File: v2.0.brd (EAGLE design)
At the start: 245 x 105 mm, 283 parts, among them J1 DC-044-A, J10 16p-2.54, J11 16p-2.54, J2 MICROSD-9P, J3 2p-2.54, J4 2p-2.54, J5 16p-2.54, J6 16p-2.54, J7 16p-2.54, J8 2p-2.54, J9 16p-2.54, Q1 32.768khZ@6Pf, Q2 SSM3J328R,LF, Q3 BSS138W-7-F, Q4 BSS138W-7-F, Q5 SSM3J328R,LF, Q6 BSS138W-7-F, Q7 BSS138W-7-F, Q8 CJ2305, SW1 MK-12C02 G1.5, SW3 MK-12C02 G1.5, SW4 MK-12C02 G1.5, SW5 TS-1101F, U1 MCP23017-E/SO, U10 74HCT139D, U11 BZX84C30, U12 SP483ECN-L, U13 FT232RL-SSOP28, U14 FT232RL-SSOP28, U15 FT232RL-SSOP28, U2 MCP79412-I/SN, U3 LOPY, U4 MAX213IDBR, U5 FT232RL-SSOP28, U6 FT232RL-SSOP28, U8 BR24G32-3, Y2 12MHZ

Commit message: Start of mods for V2
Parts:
- removed SW5: TS-1101F, Seeed-Switch-2016:SW2-5.0-6.0X3.0X4.3MM
- added SW2: MK-12C02 G1.5, Seeed-Switch:SW7-SMD-L6.7X2.7X3.2MM
- F1: device Seeed-OPL-2017-01-Fuse-Akita:TH_5MM_14MM -> imported-parts:TH_5MM_14MM
- moved J4 3.81 mm to (-15.0, 24.1)
- turned Q2 to 90 degrees
- flipped U$7 to the top
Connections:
- net +5V: now also Q2.2; no longer Q2.3
- net 5V_USB_HUB_FERRITE: now also SW2.A; no longer SW5.2
- net FTDI_HUB_LEDS: now also SW2.COM; no longer SW5.1
- net GND: now also SW2.SS1, SW2.SS2, SW2.SS3, SW2.SS4
- net N$122: now also Q2.3; no longer Q2.2
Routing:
- net GPIO4: track 81.2 -> 88.1 mm
- net LOPY_MISO: track 111.7 -> 115.5 mm
- net LOPY_3V3: track 228.5 -> 232.3 mm
- net N$123: track 11.4 -> 14.9 mm
- net N$122: track 5.47 -> 7.27 mm
- net PI_5V: track 491.2 -> 489.9 mm
- net 5V_USB_HUB_FERRITE: track 206.1 -> 204.9 mm
- net +3V3: track 672.6 -> 671.5 mm, vias 26 -> 27
- net +5V: track 434.3 -> 433.4 mm
- net FTDI_HUB_LEDS: track 60.0 -> 60.5 mm
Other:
- board text added: "3V3 Smth"
- board text added: "Pi 3V3"
- board text added: "Pi 5V"
- board text added: "SPI0"
- board text added: "V2.0"
- board text removed: "SPI8"
- board text removed: "V1.0"

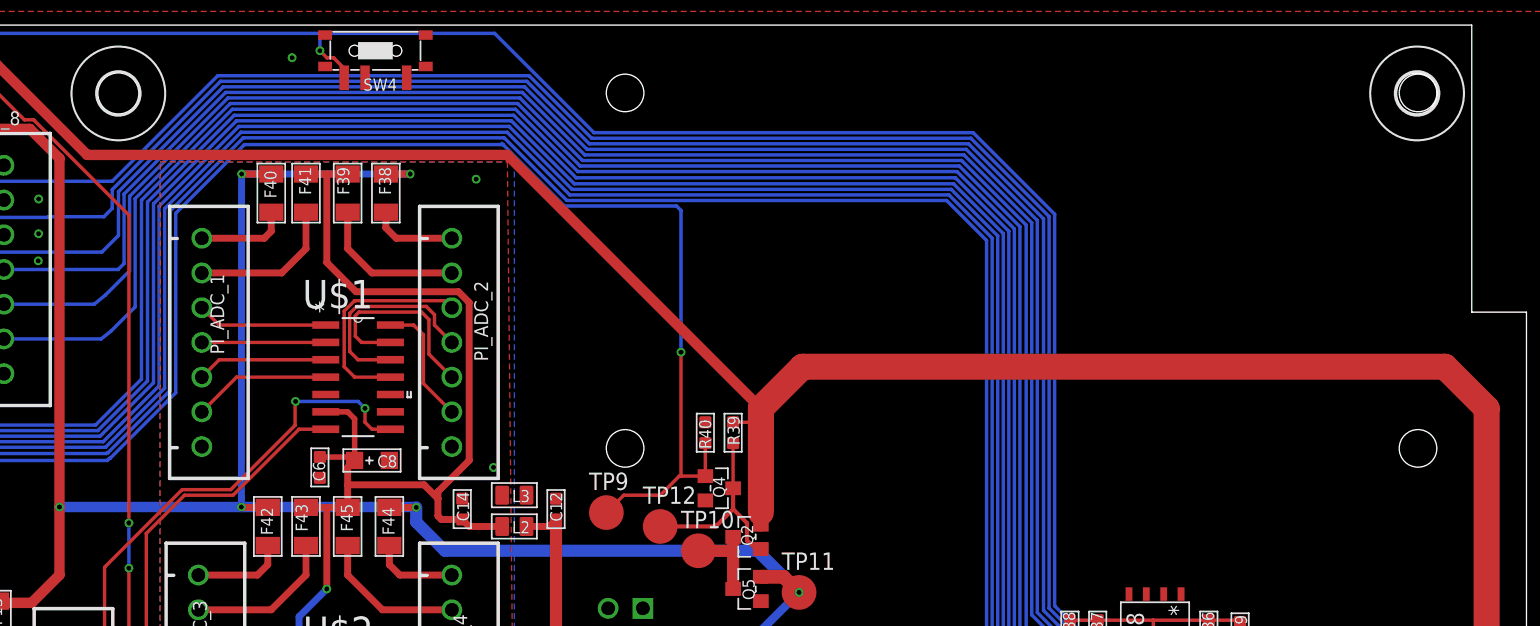
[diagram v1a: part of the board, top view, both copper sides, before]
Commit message: moved some test pads around
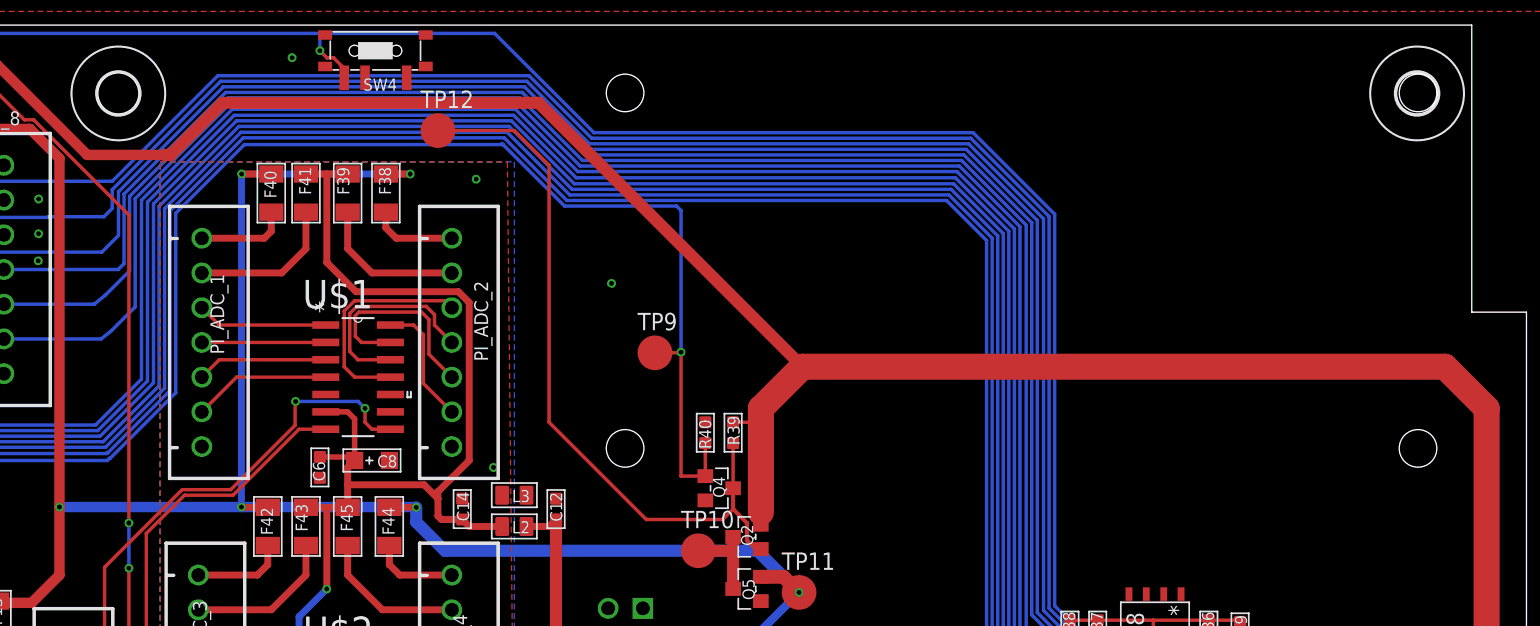
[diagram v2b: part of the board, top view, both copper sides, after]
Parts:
- moved TP12 33.2 mm to (103.4, 97.3)
- moved TP9 12.2 mm to (119.3, 81.0)
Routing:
- net N$123: track 14.9 -> 53.5 mm
- net +5V: track 433.4 -> 438.3 mm
- net PI_PWR_CTRL: track 266.4 -> 261.8 mm
- net GND: vias 46 -> 47

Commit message: More work on fixing bugs
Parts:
- added Q10, Q9: S8550, Seeed-Transistor:SOT-23
- added R26: 10K, Seeed-Resistor:R0603
- added R47: 47K, Seeed-Resistor:R0603
- moved Q8 0.51 mm to (-33.3, 32.5)
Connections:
- new net N$14: Q10.1, Q10.3, Q9.1, R26.2
- new net N$15: Q5.1, Q9.3, R47.2
- net GND: now also R26.1, R47.1; no longer Q5.1
- net LOPY_3V3: now also Q8.2; no longer Q8.3
- net LOPY_MISO: now also Q8.3; no longer Q8.2
- net N$122: now also Q10.2
- net PI_5V: now also Q9.2
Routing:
- net N$15: track 0.00 -> 8.99 mm
- net N$14: track 0.00 -> 7.88 mm
- net PI_5V: track 489.9 -> 496.5 mm, vias 6 -> 7
- net N$122: track 7.27 -> 10.3 mm
- net LOPY_3V3: track 232.3 -> 230.2 mm, vias 8 -> 9
- net LOPY_MISO: track 115.5 -> 116.9 mm

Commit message: fixed name of pycom pin 12 signal track
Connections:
- net GPIO16 renamed GPIO6

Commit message: More updates to fix issues and start of v2 BOM
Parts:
- F1: value 307010005_DIP_PPTC_4A_0310 -> (none); device imported-parts:TH_5MM_14MM -> imported-parts:2920
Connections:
- removed net LOPY_P23: J7.6, J9.6, U3.P$25
- new net LOPY_USD_SCLK: J2.5, U3.P$25
- net +24V: now also U$3.2; no longer U$3.1
- net +24V_UNREG_IN: now also F1.1; no longer F1.P$1
- net +5V: now also SW3.B
- net GND: now also U$3.1; no longer U$3.2
- net LOPY_3V3: no longer SW3.B
- net LOPY_3V3_FUSED: now also J7.6, J9.6; no longer J7.3, J9.3
- net LOPY_5V_FUSED: now also J7.3, J9.3
- net LOPY_CS1: now also J2.7; no longer LOPY_SPI.3
- net LOPY_CS2: now also LOPY_SPI.3; no longer J2.2
- net LOPY_MISO: no longer J2.7
- net LOPY_MOSI: no longer J2.3
- net LOPY_RXD1: now also J2.3
- net LOPY_SCL/CLK: no longer J2.5
- net N$68: now also F1.2; no longer F1.P$2
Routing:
- net +5V: track 438.3 -> 516.5 mm, vias 1 -> 2
- net LOPY_USD_SCLK: track 0.00 -> 46.4 mm, vias 0 -> 2
- net LOPY_RXD1: track 53.0 -> 98.2 mm, vias 0 -> 2
- net LOPY_CS2: track 19.5 -> 63.6 mm
- net LOPY_CS1: track 70.5 -> 33.6 mm, vias 0 -> 2
- net LOPY_SCL/CLK: track 97.5 -> 67.5 mm, vias 1 -> 0
- net LOPY_3V3: track 230.2 -> 200.8 mm, vias 9 -> 10
- net LOPY_MOSI: track 97.1 -> 70.9 mm, vias 1 -> 0
- net LOPY_MISO: track 116.9 -> 99.2 mm
- net LOPY_P23: track 13.7 -> 0.00 mm
- net LOPY_5V_FUSED: track 19.5 -> 24.6 mm
- net LOPY_3V3_FUSED: track 28.4 -> 33.0 mm
- net +24V: track 61.4 -> 63.9 mm
- net PI_PWR_CTRL: track 261.8 -> 264.0 mm, vias 4 -> 5
- net LED_GND: track 582.4 -> 584.4 mm
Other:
- outline, holes or cut-outs redrawn
- board text removed: "23"

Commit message: More updates, and verifing of current state of BOM
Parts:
- C31: device Seeed-Capacitor:C0805 -> Seeed-Capacitor:C0603
- C40, C44, C48: value 47uf -> 4.7uf; device Seeed-Capacitor-2016:AVX-A -> Seeed-Capacitor:AVX-A
- F1: value (none) -> 1A
- R2: value 10K 1/10W -> 10K
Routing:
- net GND: vias 47 -> 52
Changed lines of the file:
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@@
 <attribute name="VALUE" x="13.081" y="11.811" size="0.635" layer="27" ratio="10" rot="R90"/>
 </element>
-<element name="C31" library="Seeed-Capacitor" library_urn="urn:adsk.eagle:library:464" package="C0805" value="100nf" x="42.5072" y="2.282" smashed="yes" rot="R270">
-<attribute name="MPN" value="CC0805KRX7R9BB104" x="42.5072" y="2.282" size="1.778" layer="27" rot="R270" display="off"/>
+<element name="C31" library="Seeed-Capacitor" package="C0603" value="100nf" x="42.5072" y="2.282" smashed="yes" rot="R270">
+<attribute name="MPN" value="CC0603KRX7R9BB104" x="42.5072" y="2.282" size="1.778" layer="27" rot="R270" display="off"/>
 <attribute name="NAME" x="43.9042" y="2.663" size="0.889" layer="25" font="vector" ratio="11" rot="R180"/>
 <attribute name="VALUE" x="44.4122" y="4.441" size="0.635" layer="27" ratio="10" rot="R180"/>
@@
 <attribute name="VALUE" x="189.103" y="19.685" size="0.635" layer="27" ratio="10" rot="R180"/>
 </element>
-<element name="C40" library="Seeed-Capacitor-2016" package="AVX-A" value="47uf" x="10.922" y="18.796" smashed="yes" rot="R90">
-<attribute name="MPN" value="TAJA476*006#NJ" x="10.922" y="18.796" size="1.778" layer="27" rot="R90" display="off"/>
+<element name="C40" library="Seeed-Capacitor" package="AVX-A" value="4.7uf" x="10.922" y="18.796" smashed="yes" rot="R90">
+<attribute name="MPN" value="TAJA475*016#NJ" x="10.922" y="18.796" size="1.778" layer="27" rot="R90" display="off"/>
 <attribute name="NAME" x="9.906" y="17.653" size="0.889" layer="25" ratio="11" rot="R90"/>
-<attribute name="VALUE" x="13.081" y="16.891" size="0.635" layer="27" ratio="10" rot="R90"/>
+<attribute name="VALUE" value="4.7uf" x="13.081" y="16.891" size="0.635" layer="27" ratio="10" rot="R90"/>
 </element>
 <element name="C42" library="Seeed-Capacitor-2016" package="C0603" value="100nf" x="4.318" y="39.878" smashed="yes" rot="R270">
@@
 <attribute name="VALUE" x="0.3175" y="32.004" size="0.635" layer="27" ratio="10" rot="R90"/>
 </element>
-<element name="C44" library="Seeed-Capacitor-2016" package="AVX-A" value="47uf" x="4.318" y="37.846" smashed="yes">
-<attribute name="MPN" value="TAJA476*006#NJ" x="4.318" y="37.846" size="1.778" layer="27" display="off"/>
+<element name="C44" library="Seeed-Capacitor" package="AVX-A" value="4.7uf" x="4.318" y="37.846" smashed="yes">
+<attribute name="MPN" value="TAJA475*016#NJ" x="4.318" y="37.846" size="1.778" layer="27" display="off"/>
 <attribute name="NAME" x="6.985" y="37.338" size="0.889" layer="25" ratio="11"/>
-<attribute name="VALUE" x="2.413" y="35.687" size="0.635" layer="27" ratio="10"/>
+<attribute name="VALUE" value="4.7uf" x="2.413" y="35.687" size="0.635" layer="27" ratio="10"/>
 </element>
 <element name="C46" library="Seeed-Capacitor-2016" package="C0603" value="100nf" x="18.034" y="40.386" smashed="yes" rot="R270">
@@
 <attribute name="VALUE" x="10.668" y="31.9405" size="0.635" layer="27" ratio="10"/>
 </element>
-<element name="C48" library="Seeed-Capacitor-2016" package="AVX-A" value="47uf" x="18.034" y="38.354" smashed="yes">
-<attribute name="MPN" value="TAJA476*006#NJ" x="18.034" y="38.354" size="1.778" layer="27" display="off"/>
+<element name="C48" library="Seeed-Capacitor" package="AVX-A" value="4.7uf" x="18.034" y="38.354" smashed="yes">
+<attribute name="MPN" value="TAJA475*016#NJ" x="18.034" y="38.354" size="1.778" layer="27" display="off"/>
 <attribute name="NAME" x="13.335" y="37.846" size="0.889" layer="25" ratio="11"/>
-<attribute name="VALUE" x="16.129" y="36.195" size="0.635" layer="27" ratio="10"/>
+<attribute name="VALUE" value="4.7uf" x="16.129" y="36.195" size="0.635" layer="27" ratio="10"/>
 </element>
 <element name="C6" library="Seeed-Capacitor-2016" library_urn="urn:adsk.eagle:library:450" package="C0603" value="100nf" x="94.742" y="72.644" smashed="yes" rot="R180">
@@
 <attribute name="VALUE" x="88.5825" y="22.987" size="0.635" layer="27" ratio="10" rot="R270"/>
 </element>
-<element name="F1" library="imported-parts" package="2920" value="" x="182.626" y="35.306" rot="R270"/>
+<element name="F1" library="imported-parts" package="2920" value="1A" x="182.626" y="35.306" rot="R270"/>
 <element name="F2" library="Seeed-Fuse" library_urn="urn:adsk.eagle:library:469" package="F1206" value="SMD1206R500SF" x="-0.508" y="96.012" smashed="yes" rot="R270">
 <attribute name="MPN" value="SMD1206R500SF" x="-0.508" y="96.012" size="1.778" layer="27" rot="R270" display="off"/>
@@
 <attribute name="VALUE" x="123.025" y="59.009" size="0.635" layer="27" ratio="10" rot="R270"/>
 </element>
-<element name="R2" library="Seeed-Resistor" library_urn="urn:adsk.eagle:library:474" package="R0603" value="10K 1/10W" x="143.51" y="25.4" smashed="yes" rot="R180">
-<attribute name="MPN" value="RC0603JR-0710KL" x="143.51" y="25.4" size="1.778" layer="27" rot="R180" display="off"/>
+<element name="R2" library="Seeed-Resistor" package="R0603" value="10K" x="143.51" y="25.4" smashed="yes" rot="R180">
+<attribute name="MPN" value="RC0603FR-0710KL" x="143.51" y="25.4" size="1.778" layer="27" rot="R180" display="off"/>
 <attribute name="NAME" x="143.002" y="26.543" size="0.889" layer="25" ratio="11" rot="R270"/>
-<attribute name="VALUE" x="142.075" y="27.005" size="0.635" layer="27" ratio="10" rot="R270"/>
+<attribute name="VALUE" value="10K" x="142.075" y="27.005" size="0.635" layer="27" ratio="10" rot="R270"/>
 </element>
 <element name="R20" library="Seeed-Resistor" library_urn="urn:adsk.eagle:library:474" package="R0603" value="15K 1/10W" x="183.134" y="20.066" smashed="yes" rot="R90">
@@
 <contactref element="R26" pad="1"/>
 <contactref element="R47" pad="1"/>
+<via x="142.24" y="54.61" extent="1-16" drill="0.35"/>
+<via x="147.066" y="60.071" extent="1-16" drill="0.35"/>
+<via x="123.571" y="38.989" extent="1-16" drill="0.35"/>
+<via x="125.857" y="38.608" extent="1-16" drill="0.35"/>
+<via x="125.73" y="27.686" extent="1-16" drill="0.35"/>
 </signal>
 <signal name="+3V3">
@@
 <wire x1="21.082" y1="9.906" x2="20.574" y2="10.414" width="0.254" layer="1"/>
 <wire x1="23.114" y1="8.128" x2="21.844" y2="8.128" width="0.254" layer="1"/>
-<wire x1="41.6182" y1="2.282" x2="41.6182" y2="1.9942" width="0.254" layer="1"/>
+<wire x1="41.7452" y1="2.282" x2="41.6182" y2="1.9942" width="0.254" layer="1"/>
 <wire x1="41.6182" y1="1.9942" x2="40.386" y2="0.762" width="0.254" layer="1"/>
 <wire x1="22.4412" y1="19.427" x2="23.753" y2="19.427" width="0.254" layer="1"/>
@@
 <contactref element="SW2" pad="A"/>
 <wire x1="46.736" y1="3.756" x2="43.0922" y2="3.756" width="0.254" layer="1"/>
-<wire x1="43.0922" y1="3.756" x2="41.6182" y2="2.282" width="0.254" layer="1"/>
+<wire x1="43.0922" y1="3.756" x2="41.7452" y2="2.282" width="0.254" layer="1"/>
 </signal>
 <signal name="N$49">

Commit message: Lopy reset and bootloader now on port expander
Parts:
- added F56, F57: SMD1206R500SF, Seeed-Fuse:F1206
- moved R2 23.8 mm to (120.0, 21.5)
- moved J6 4.83 mm to (134.9, 5.59), turned to 270 degrees
- moved J5 3.17 mm to (134.9, 2.16), turned to 270 degrees
- moved R8 0.89 mm to (-31.8, 56.0)
- moved R41 0.25 mm to (-30.2, 48.8), turned to 0 degrees
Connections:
- removed net GPIO_3V3_FUSED: F62.2, J10.4, J10.5, J10.6, J11.4, J11.5, J11.6
- removed net GPIO_EXP_0: J5.1, J6.1, U1.21
- removed net GPIO_EXP_1: J5.2, J6.2, U1.22
- removed net GPIO_EXP_10: J5.11, J6.11, U1.3
- removed net GPIO_EXP_11: J5.12, J6.12, U1.4
- removed net GPIO_EXP_12: J5.13, J6.13, U1.5
- removed net GPIO_EXP_13: J5.14, J6.14, U1.6
- removed net GPIO_EXP_14: J5.15, J6.15, U1.7
- removed net GPIO_EXP_15: J5.16, J6.16, U1.8
- removed net GPIO_EXP_2: J5.3, J6.3, U1.23
- removed net GPIO_EXP_3: J5.4, J6.4, U1.24
- removed net GPIO_EXP_4: J5.5, J6.5, U1.25
- removed net GPIO_EXP_5: J5.6, J6.6, U1.26
- removed net GPIO_EXP_6: J5.7, J6.7, U1.27
- removed net GPIO_EXP_7: J5.8, J6.8, U1.28
- removed net GPIO_EXP_8: J5.9, J6.9, U1.1
- removed net GPIO_EXP_9: J5.10, J6.10, U1.2
- new net EXP_3V3: F56.1, J5.2, J6.2
- new net EXP_5V: F57.1, J5.1, J6.1
- new net GPA0: J5.3, J6.3, U1.21
- new net GPA1: J5.4, J6.4, U1.22
- new net GPA2: J5.5, J6.5, U1.23
- new net GPA3: J5.6, J6.6, U1.24
- new net GPA4: J5.7, J6.7, U1.25
- new net GPA5: J5.8, J6.8, U1.26
- new net GPA6: J5.9, J6.9, U1.27
- new net GPA7: J5.10, J6.10, U1.28
- new net GPB0: J5.11, J6.11, U1.1
- new net GPB1: J5.12, J6.12, U1.2
- new net GPB2: J5.13, J6.13, U1.3
- new net GPB3: J5.14, J6.14, U1.4
- new net GPB4: J5.15, J6.15, U1.5
- new net GPIO26: J10.14, J11.14, PCB1.P$37
- new net N$16: R41.1, U1.6
- new net N$18: R17.1, U1.7
- new net N$19: F62.2, J10.3, J10.4, J11.3, J11.4
- net +3V3: now also F56.2
- net GND: now also J5.16, J6.16; no longer J10.14, J11.14
- net GPIO5: now also J10.5, J11.5; no longer R41.2
- net GPIO6: now also J10.6, J11.6; no longer R17.2
- net GPIO_5V_FUSED: no longer J10.3, J11.3
- net LOPY_RST_EN: now also U1.8; no longer PCB1.P$37
- net P12_SIG: now also R17.2; no longer R17.1
- net P2_SIG: now also R41.2; no longer R41.1
- net PI_5V: now also F57.2
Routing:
- net N$18: track 0.00 -> 403.7 mm, vias 0 -> 2
- net N$16: track 0.00 -> 378.5 mm, vias 0 -> 2
- net GPIO6: track 305.5 -> 47.7 mm
- net GPIO5: track 266.9 -> 46.4 mm
- net LOPY_RST_EN: track 267.8 -> 367.8 mm, vias 3 -> 4
- net GPIO_EXP_8: track 51.6 -> 0.00 mm
- net GPIO_EXP_9: track 48.8 -> 0.00 mm
- net GPB4: track 0.00 -> 48.3 mm
- net GPIO_EXP_10: track 45.5 -> 0.00 mm
- net GPB3: track 0.00 -> 43.6 mm
- net GPIO_EXP_11: track 41.8 -> 0.00 mm
- net PI_5V: track 496.5 -> 536.8 mm, vias 7 -> 9
- net GPIO_EXP_0: track 40.1 -> 0.00 mm
- net GPIO_EXP_12: track 39.0 -> 0.00 mm
- net GPIO26: track 0.00 -> 39.0 mm
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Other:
- board text added: "26"
- board text added: "GPA0"
- board text added: "GPA1"
- board text added: "GPA2"
- board text added: "GPA3"
- board text added: "GPA4"
- board text added: "GPA5"
- board text added: "GPA6"
- board text added: "GPA7"
- board text added: "GPB0"
- board text added: "GPB1"
- board text added: "GPB2"
- board text added: "GPB3"
- board text added: "GPB4"
- board text removed: "0"
- board text removed: "1"
- board text removed: "10"
- board text removed: "11"
- board text removed: "12"
- board text removed: "13"
- board text removed: "14"
- board text removed: "2"
- board text removed: "3"
- board text removed: "4"
- board text removed: "5"
- board text removed: "6"
- board text removed: "7"
- board text removed: "8"
- board text removed: "9"
